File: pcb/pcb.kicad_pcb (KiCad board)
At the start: 2 copper layers, 76 x 100 mm, 27 parts, among them J1 Screw_Terminal_01x06, J10 Screw_Terminal_01x04, J2 male header, J3 Screw_Terminal_01x07, J4 Screw_Terminal_01x02, J5 Screw_Terminal_01x04, J6 JST XH-2P, J7 JST XH-3P, J8 JST XH-4P, J9 Screw_Terminal_01x04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

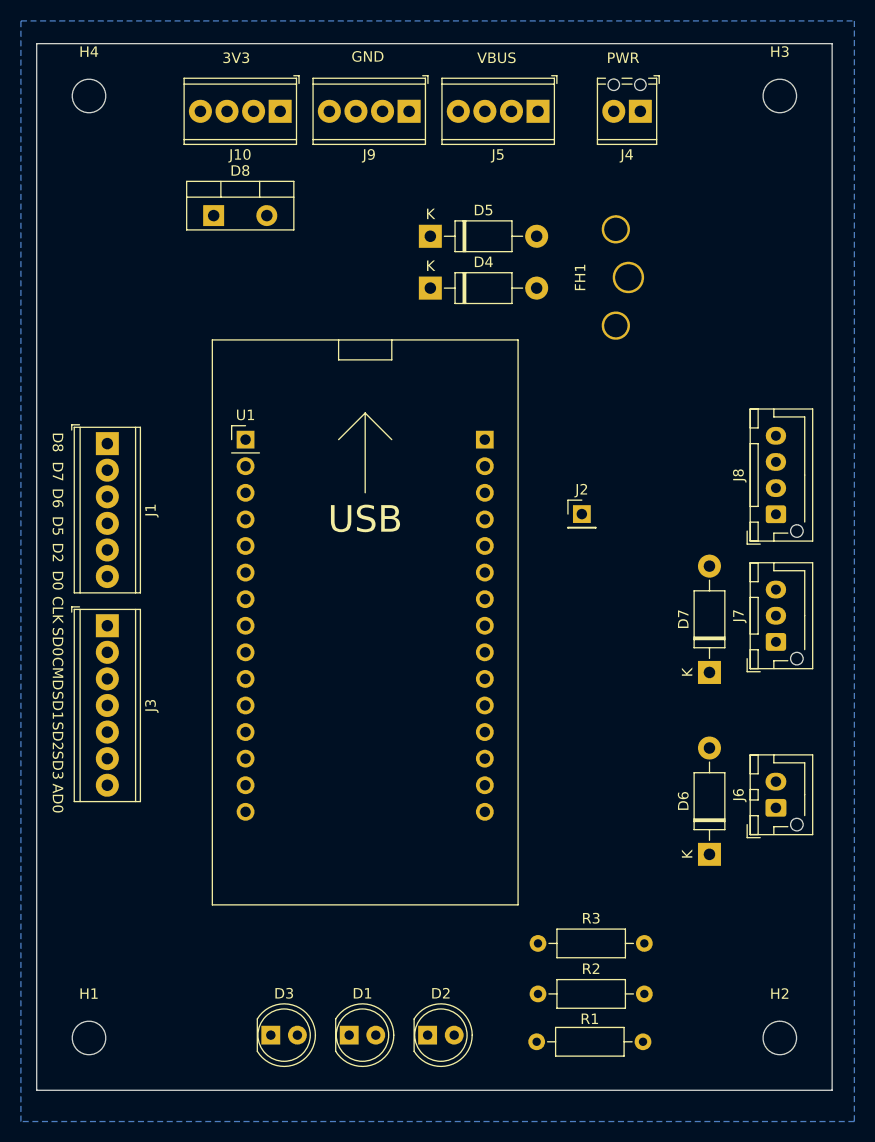
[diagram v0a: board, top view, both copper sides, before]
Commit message: Route door controller pcb
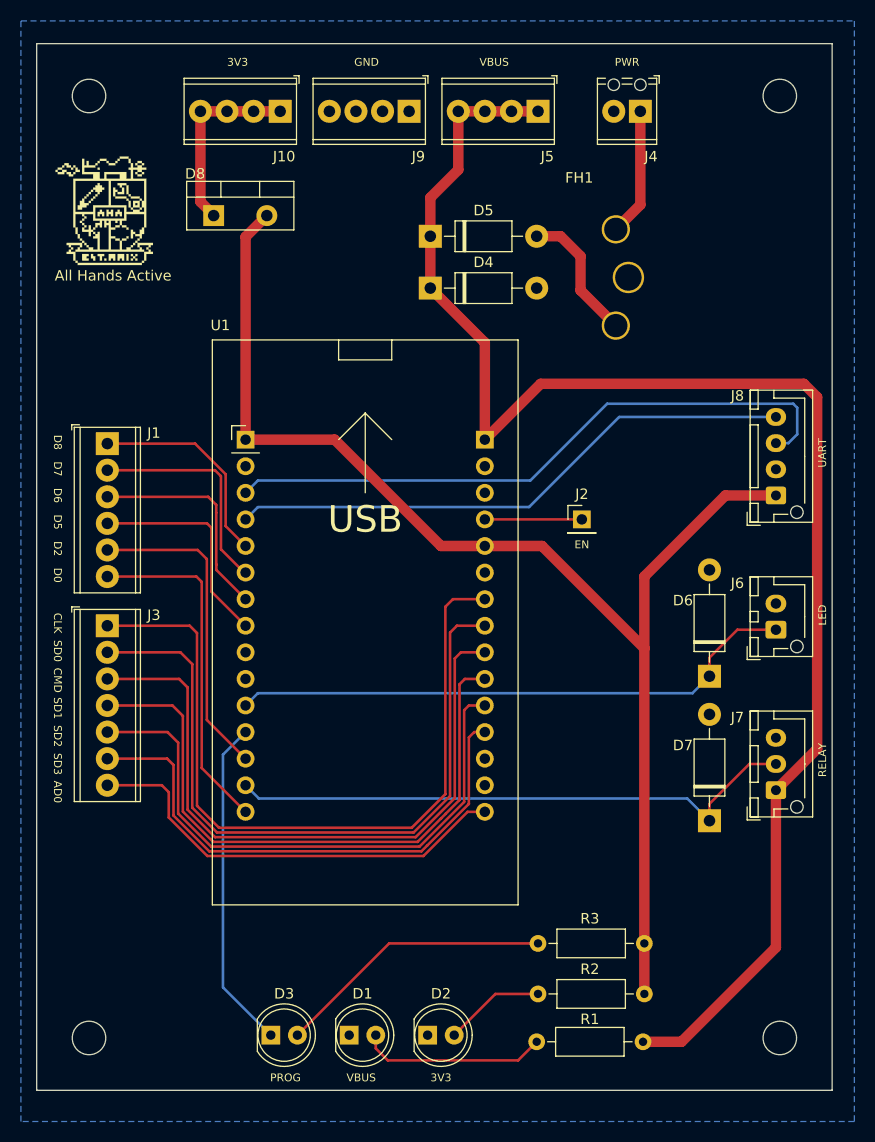
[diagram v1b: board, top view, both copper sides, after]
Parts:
- moved D6 17.0 mm to (208.3, 99.4)
- moved J6 17.0 mm to (214.6, 95.0)
- moved D7 14.2 mm to (208.3, 113.2)
- moved J7 14.2 mm to (214.6, 110.3)
- moved J8 1.80 mm to (214.6, 82.2)
- moved J2 0.51 mm to (196.1, 84.5)
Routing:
- net VBUS: track 0.00 -> 147.4 mm
- net +3V3: track 0.00 -> 124.3 mm
- net Net-(J3-Pad1): track 0.00 -> 73.3 mm
- net Net-(J3-Pad2): track 0.00 -> 68.6 mm
- net Net-(J3-Pad3): track 0.00 -> 64.3 mm
- net /TXD: track 0.00 -> 61.3 mm
- net Net-(J3-Pad4): track 0.00 -> 59.7 mm
- net Net-(J3-Pad5): track 0.00 -> 55.3 mm
- net /UNLOCK_PIN: track 0.00 -> 55.3 mm
- net /RXD: track 0.00 -> 54.7 mm
- net /UNLOCK_LED: track 0.00 -> 54.7 mm
- net Net-(J3-Pad6): track 0.00 -> 51.0 mm
- net Net-(J3-Pad7): track 0.00 -> 42.0 mm
- net Net-(J1-Pad6): track 0.00 -> 32.9 mm
- net /GPIO_0: track 0.00 -> 31.7 mm
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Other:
- board text added: "All Hands Active"
- board text removed: "3V3"
- board text removed: "GND"
- board text removed: "PWR"
- board text removed: "VBUS"

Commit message: Added second relay and LED connectors to the PCB to allow controlling of two doors
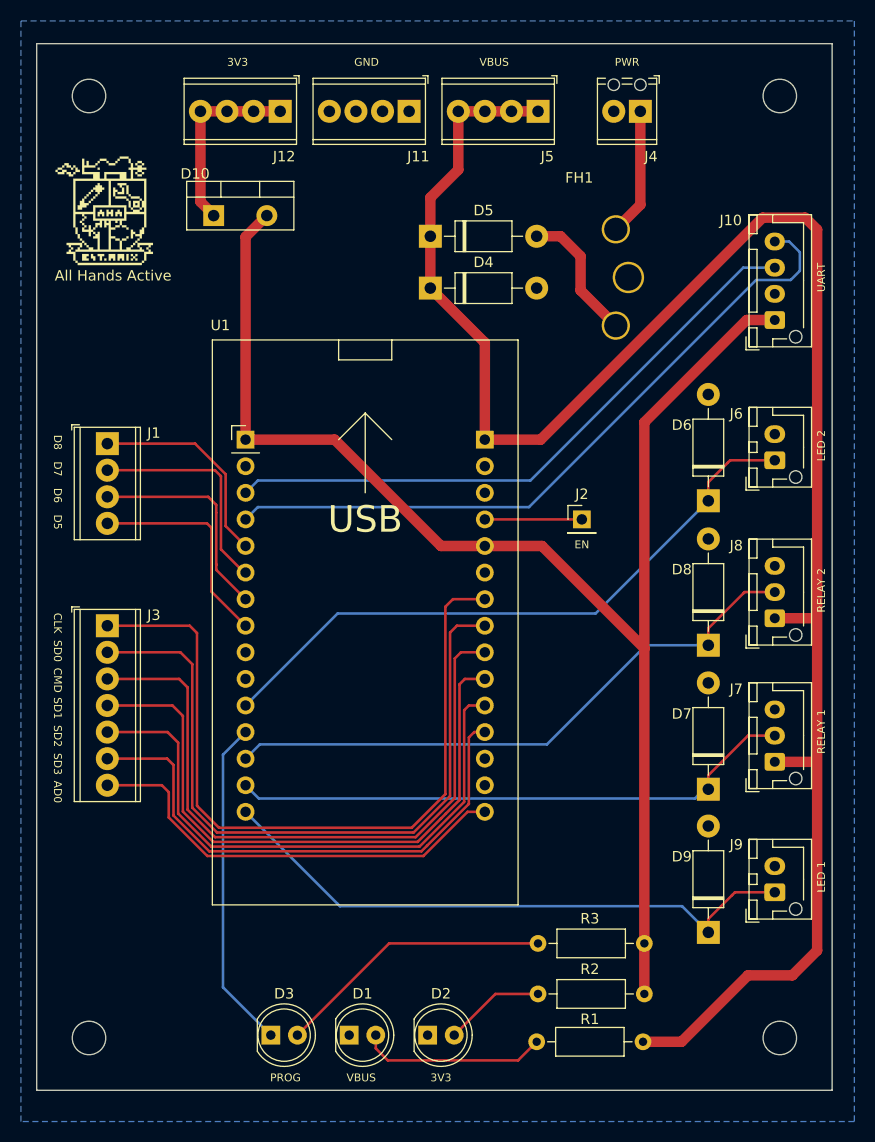
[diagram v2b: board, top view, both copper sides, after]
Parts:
- added D8: 1N4728A-TR, Diode_THT:D_DO-41_SOD81_P10.16mm_Horizontal, F.Cu at (208.2, 96.5)
- added D9: 1N4728A-TR, Diode_THT:D_DO-41_SOD81_P10.16mm_Horizontal, F.Cu at (208.2, 123.9)
- added J8: JST XH-3P, Connector_JST:JST_XH_B3B-XH-AM_1x03_P2.50mm_Vertical, F.Cu at (214.5, 93.9)
- added J9: JST XH-2P, Connector_JST:JST_XH_B2B-XH-AM_1x02_P2.50mm_Vertical, F.Cu at (214.5, 120.1)
- J1: footprint TerminalBlock_Phoenix:TerminalBlock_Phoenix_MPT-0,5-6-2.54_1x06_P2.54mm_Horizontal -> TerminalBlock_Phoenix:TerminalBlock_Phoenix_MPT-0,5-4-2.54_1x04_P2.54mm_Horizontal
- moved D6 16.8 mm to (208.2, 82.7)
- moved J10 16.8 mm to (214.5, 65.4)
- moved J6 16.2 mm to (214.5, 78.8)
- moved D7 3.01 mm to (208.2, 110.2)
- moved J7 2.71 mm to (214.5, 107.6)
- renumbered D8 to D10, J8 to J10, J9 to J11, J10 to J12
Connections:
- net /UNLOCK_LED renamed /UNLOCK1_LED
- net /UNLOCK_PIN renamed /UNLOCK1_PIN
- U1 pad 13: Net-(J1-Pad5) -> /UNLOCK2_PIN
- U1 pad 15: Net-(J1-Pad6) -> /UNLOCK2_LED
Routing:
- net /UNLOCK2_PIN: track 0.00 -> 58.1 mm
- net /UNLOCK2_LED: track 0.00 -> 57.7 mm
- net Net-(J1-Pad6): track 32.9 -> 0.00 mm
- net VBUS: track 147.4 -> 180.3 mm
- net Net-(J1-Pad5): track 30.5 -> 0.00 mm
- net +3V3: track 124.3 -> 139.7 mm
- net /RXD: track 54.7 -> 67.4 mm
- net /UNLOCK1_LED: track 54.7 -> 61.3 mm
- net /TXD: track 61.3 -> 59.5 mm
- net /UNLOCK1_PIN: track 55.3 -> 54.4 mm
